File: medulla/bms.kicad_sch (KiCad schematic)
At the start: 35 parts, among them Q1 CSD18534Q5A, Q2 CSD18534Q5A, U1 BQ7791504PW

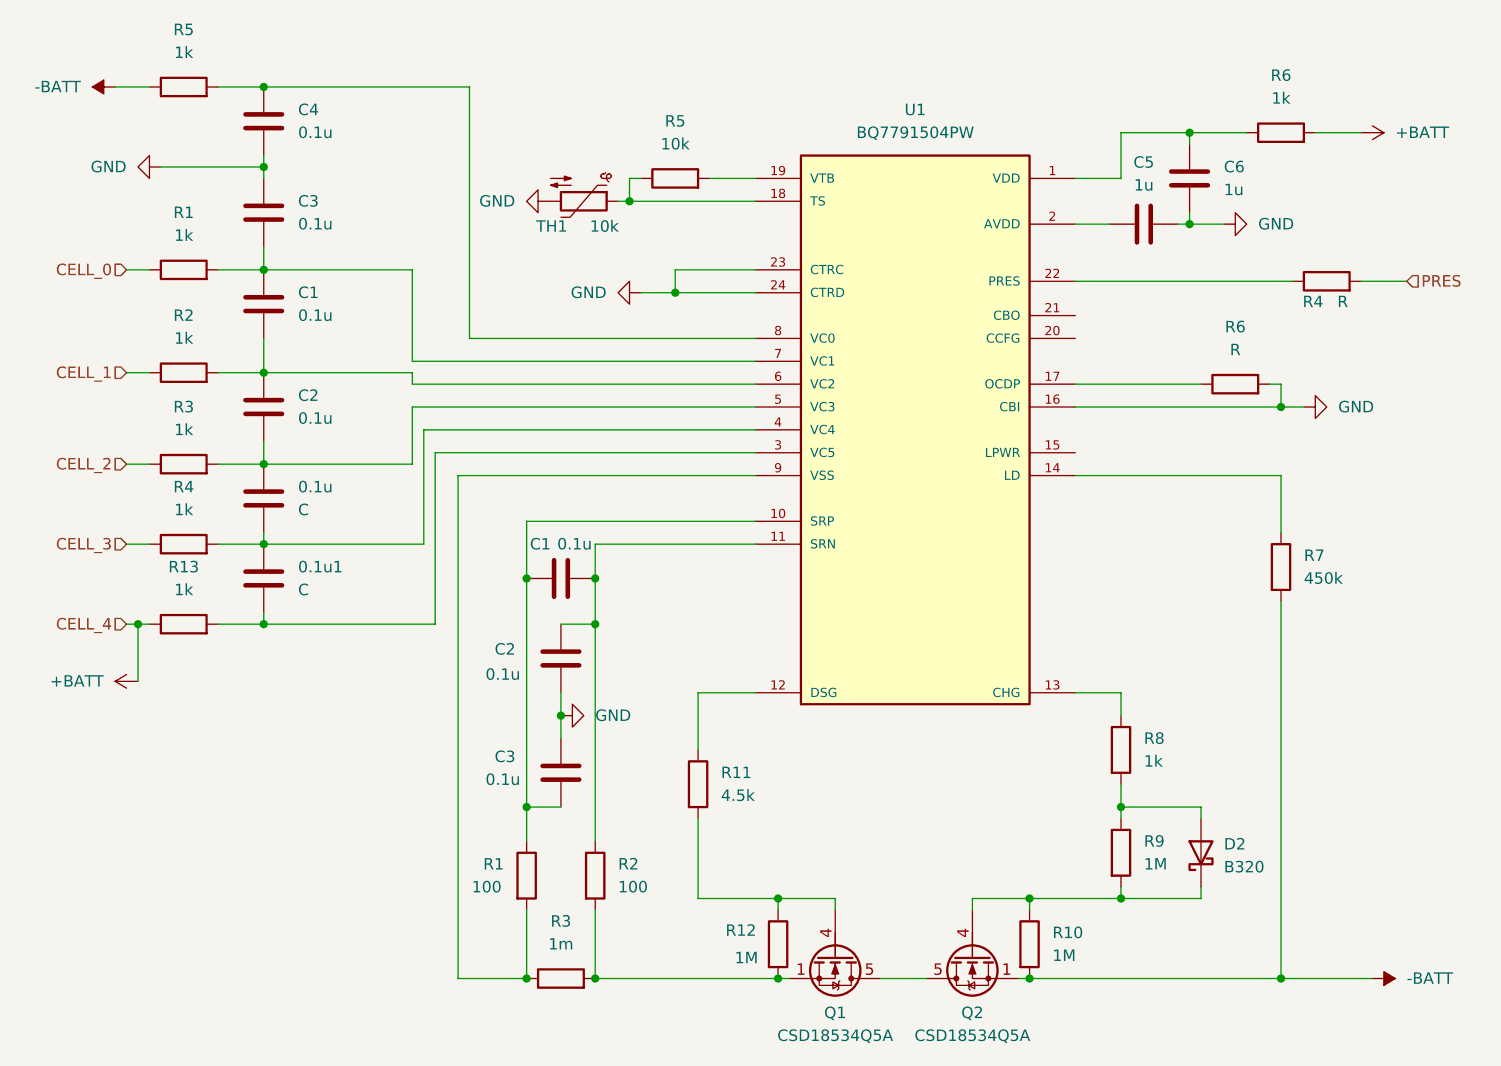
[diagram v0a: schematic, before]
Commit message: 0.1.3-alpha: H-Bridge Completion & I2C Sensor integration
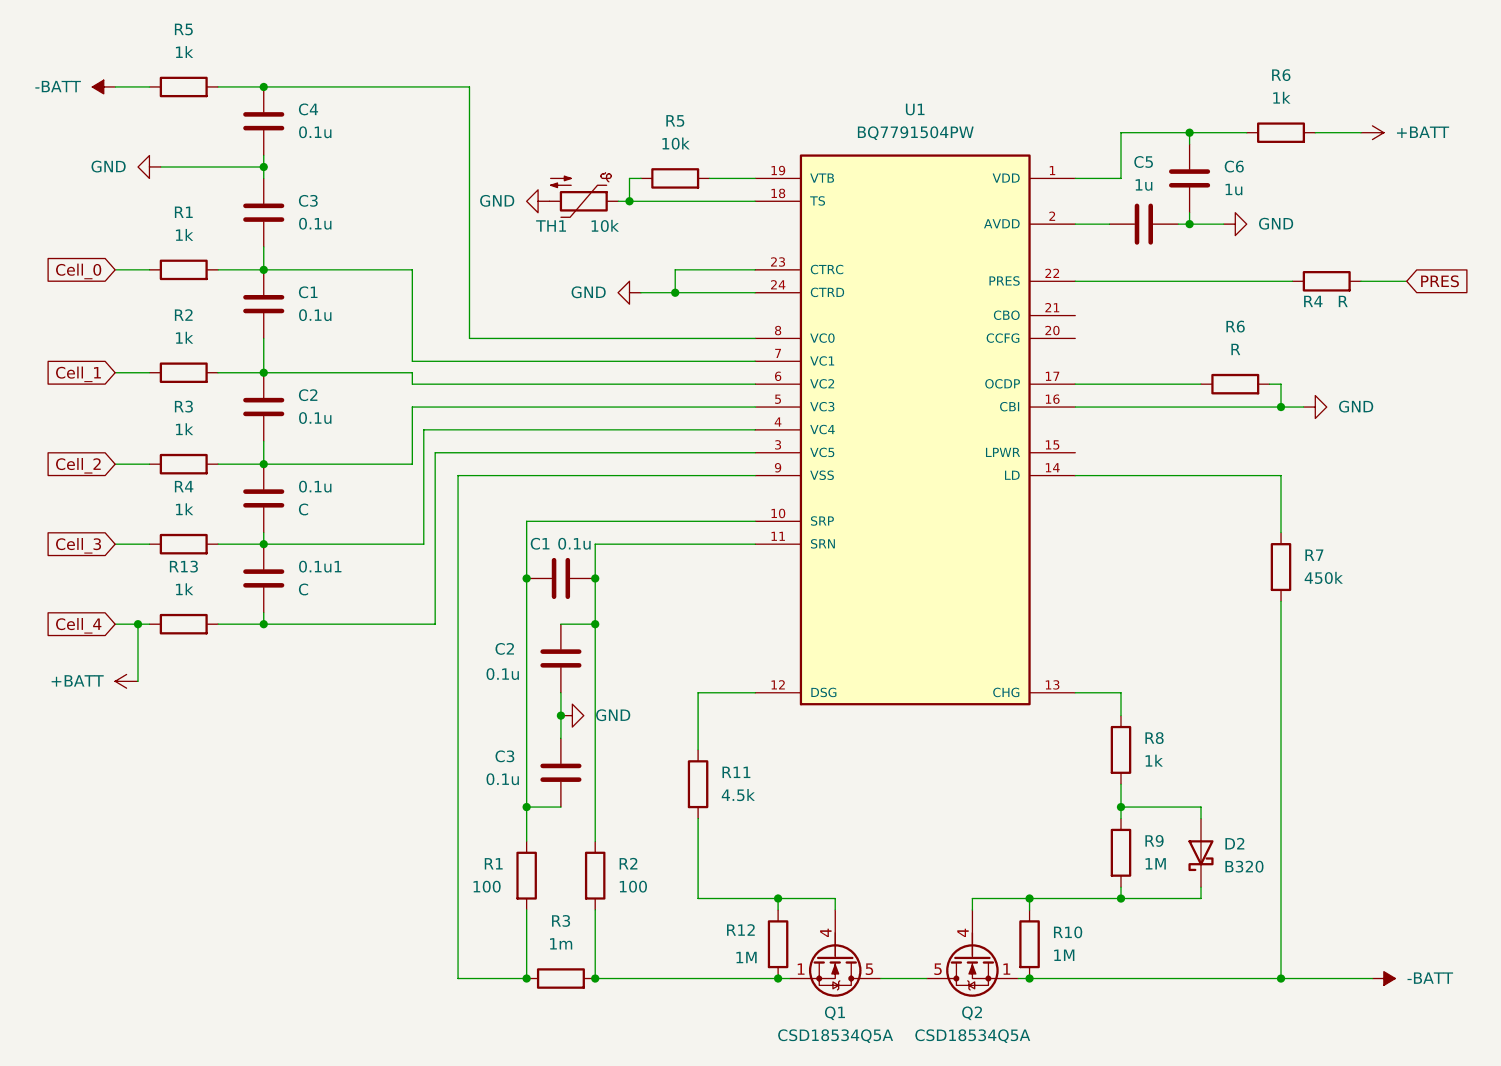
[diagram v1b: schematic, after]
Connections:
- net CELL_0 renamed Cell_0
- net CELL_1 renamed Cell_1
- net CELL_2 renamed Cell_2
- net CELL_3 renamed Cell_3
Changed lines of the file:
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@@
-	(wire
-		(pts
-			(xy 48.26 72.39) (xy 50.8 72.39)
-		)
-		(stroke
-			(width 0)
-			(type default)
-		)
-	)
 	(wire
 		(pts
@@
 	(wire
 		(pts
+			(xy 46.99 83.82) (xy 50.8 83.82)
+		)
+		(stroke
+			(width 0)
+			(type default)
+		)
+	)
+	(wire
+		(pts
 			(xy 158.75 140.97) (xy 158.75 142.24)
 		)
@@
 	(wire
 		(pts
-			(xy 48.26 111.76) (xy 49.53 111.76)
+			(xy 46.99 93.98) (xy 50.8 93.98)
 		)
 		(stroke
@@
 	(wire
 		(pts
-			(xy 48.26 93.98) (xy 50.8 93.98)
-		)
-		(stroke
-			(width 0)
-			(type default)
-		)
-	)
-	(wire
-		(pts
 			(xy 58.42 52.07) (xy 63.5 52.07)
 		)
@@
 	(wire
 		(pts
-			(xy 48.26 83.82) (xy 50.8 83.82)
-		)
-		(stroke
-			(width 0)
-			(type default)
-		)
-	)
-	(wire
-		(pts
 			(xy 85.09 151.13) (xy 92.71 151.13)
 		)
@@
 	(wire
 		(pts
+			(xy 46.99 102.87) (xy 50.8 102.87)
+		)
+		(stroke
+			(width 0)
+			(type default)
+		)
+	)
+	(wire
+		(pts
 			(xy 92.71 100.33) (xy 92.71 106.68)
 		)
@@
 	(wire
 		(pts
+			(xy 46.99 111.76) (xy 49.53 111.76)
+		)
+		(stroke
+			(width 0)
+			(type default)
+		)
+	)
+	(wire
+		(pts
 			(xy 158.75 129.54) (xy 158.75 132.08)
 		)
@@
 	(wire
 		(pts
-			(xy 48.26 102.87) (xy 50.8 102.87)
+			(xy 46.99 72.39) (xy 50.8 72.39)
 		)
 		(stroke
@@
 		)
 	)
-	(hierarchical_label "CELL_1"
+	(global_label "Cell_3"
 		(shape input)
-		(at 48.26 83.82 180)
+		(at 46.99 102.87 180)
+		(fields_autoplaced yes)
 		(effects
 			(font
@@
 			(justify right)
 		)
-	)
-	(hierarchical_label "PRES"
+		(property "Intersheetrefs" "${INTERSHEET_REFS}"
+			(at 38.1387 102.87 0)
+			(effects
+				(font
+					(size 1.27 1.27)
+				)
+				(justify right)
+				(hide yes)
+			)
+		)
+	)
+	(global_label "Cell_1"
 		(shape input)
-		(at 190.5 73.66 0)
+		(at 46.99 83.82 180)
+		(fields_autoplaced yes)
 		(effects
 			(font
 				(size 1.27 1.27)
 			)
-			(justify left)
-		)
-	)
-	(hierarchical_label "CELL_0"
+			(justify right)
+		)
+		(property "Intersheetrefs" "${INTERSHEET_REFS}"
+			(at 38.1387 83.82 0)
+			(effects
+				(font
+					(size 1.27 1.27)
+				)
+				(justify right)
+				(hide yes)
+			)
+		)
+	)
+	(global_label "PRES"
 		(shape input)
-		(at 48.26 72.39 180)
+		(at 190.5 73.66 0)
+		(fields_autoplaced yes)
 		(effects
 			(font
 				(size 1.27 1.27)
 			)
-			(justify right)
-		)
-	)
-	(hierarchical_label "CELL_3"
+			(justify left)
+		)
+		(property "Intersheetrefs" "${INTERSHEET_REFS}"
+			(at 198.3837 73.66 0)
+			(effects
+				(font
+					(size 1.27 1.27)
+				)
+				(justify left)
+				(hide yes)
+			)
+		)
+	)
+	(global_label "Cell_4"
 		(shape input)
-		(at 48.26 102.87 180)
+		(at 46.99 111.76 180)
+		(fields_autoplaced yes)
 		(effects
 			(font
@@
 			(justify right)
 		)
-	)
-	(hierarchical_label "CELL_4"
+		(property "Intersheetrefs" "${INTERSHEET_REFS}"
+			(at 38.1387 111.76 0)
+			(effects
+				(font
+					(size 1.27 1.27)
+				)
+				(justify right)
+				(hide yes)
+			)
+		)
+	)
+	(global_label "Cell_2"
 		(shape input)
-		(at 48.26 111.76 180)
+		(at 46.99 93.98 180)
+		(fields_autoplaced yes)
 		(effects
 			(font
@@
 			(justify right)
 		)
-	)
-	(hierarchical_label "CELL_2"
+		(property "Intersheetrefs" "${INTERSHEET_REFS}"
+			(at 38.1387 93.98 0)
+			(effects
+				(font
+					(size 1.27 1.27)
+				)
+				(justify right)
+				(hide yes)
+			)
+		)
+	)
+	(global_label "Cell_0"
 		(shape input)
-		(at 48.26 93.98 180)
+		(at 46.99 72.39 180)
+		(fields_autoplaced yes)
 		(effects
 			(font
@@
 			(justify right)
 		)
-	)
+		(property "Intersheetrefs" "${INTERSHEET_REFS}"
+			(at 38.1387 72.39 0)
+			(effects
+				(font
+					(size 1.27 1.27)
+				)
+				(justify right)
+				(hide yes)
+			)
+		)
+	)
